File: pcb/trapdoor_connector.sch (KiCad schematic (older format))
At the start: 1 part, among them X1 A1200_trapdoor_connector

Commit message: Some work done on the whole project
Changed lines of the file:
@@
 Text Label 1100 5800 0    50   ~ 0
 _BR
-Text Label 3800 1800 0    50   ~ 0
+Text Label 3850 1800 0    50   ~ 0
 D31
-Text Label 3800 1900 0    50   ~ 0
+Text Label 3850 1900 0    50   ~ 0
 D30
-Text Label 3800 2000 0    50   ~ 0
+Text Label 3850 2000 0    50   ~ 0
 D29
 Text Label 3800 2100 0    50   ~ 0
@@
 	1    0    0    -1
 $EndComp
-Text HLabel 900  700  0    50   BiDi ~ 0
-TRPDR
-Text Label 7550 5300 0    50   ~ 0
-+5VDC
-Text Label 7550 5200 0    50   ~ 0
-+5VDC
-Text Label 7550 5100 0    50   ~ 0
-+5VDC
-Text Label 7550 4900 0    50   ~ 0
-+5VDC
-Text Label 7550 5000 0    50   ~ 0
-+5VDC
-Text Label 7550 4800 0    50   ~ 0
-+5VDC
-Text Label 7550 4700 0    50   ~ 0
-+5VDC
-Text Label 7550 4600 0    50   ~ 0
-+5VDC
-Text Label 7550 4500 0    50   ~ 0
-+5VDC
-Text Label 7550 4400 0    50   ~ 0
-+5VDC
-Text Label 7550 4300 0    50   ~ 0
+Text Label 7850 5300 0    50   ~ 0
++5VDC
+Text Label 7850 5200 0    50   ~ 0
++5VDC
+Text Label 7850 5100 0    50   ~ 0
++5VDC
+Text Label 7850 4900 0    50   ~ 0
++5VDC
+Text Label 7850 5000 0    50   ~ 0
++5VDC
+Text Label 7850 4800 0    50   ~ 0
++5VDC
+Text Label 7850 4700 0    50   ~ 0
++5VDC
+Text Label 7850 4600 0    50   ~ 0
++5VDC
+Text Label 7850 4500 0    50   ~ 0
++5VDC
+Text Label 7850 4400 0    50   ~ 0
++5VDC
+Text Label 7850 4300 0    50   ~ 0
 +5VDC
 Text Label 5050 5300 0    50   ~ 0
@@
 	4900 4700 5000 4800
 Wire Wire Line
-	7550 5300 7800 5300
-Wire Wire Line
-	7800 5200 7550 5200
-Wire Wire Line
-	7550 5100 7800 5100
-Wire Wire Line
-	7800 5000 7550 5000
-Wire Wire Line
-	7550 4900 7800 4900
-Wire Wire Line
-	7800 4800 7550 4800
-Wire Wire Line
-	7550 4700 7800 4700
-Wire Wire Line
-	7800 4600 7550 4600
-Wire Wire Line
-	7550 4500 7800 4500
-Wire Wire Line
-	7800 4400 7550 4400
-Wire Wire Line
-	7550 4300 7800 4300
+	7550 5300 8450 5300
+Wire Wire Line
+	8450 5200 7550 5200
+Wire Wire Line
+	7550 5100 8450 5100
+Wire Wire Line
+	8450 5000 7550 5000
+Wire Wire Line
+	7550 4900 8450 4900
+Wire Wire Line
+	8450 4800 7550 4800
+Wire Wire Line
+	7550 4700 8450 4700
+Wire Wire Line
+	8450 4600 7550 4600
+Wire Wire Line
+	7550 4500 8450 4500
+Wire Wire Line
+	8450 4400 7550 4400
+Wire Wire Line
+	7550 4300 8450 4300
 Wire Wire Line
 	5000 5300 5350 5300
@@
 	5000 4300 5350 4300
 Wire Bus Line
-	4900 3900 7900 3900
-Entry Wire Line
-	7800 5300 7900 5400
-Entry Wire Line
-	7800 5200 7900 5300
-Entry Wire Line
-	7800 5100 7900 5200
-Entry Wire Line
-	7800 5000 7900 5100
-Entry Wire Line
-	7800 4900 7900 5000
-Entry Wire Line
-	7800 4800 7900 4900
-Entry Wire Line
-	7800 4700 7900 4800
-Entry Wire Line
-	7800 4600 7900 4700
-Entry Wire Line
-	7800 4500 7900 4600
-Entry Wire Line
-	7800 4400 7900 4500
-Entry Wire Line
-	7800 4300 7900 4400
+	4900 3900 8550 3900
+Entry Wire Line
+	8450 5300 8550 5400
+Entry Wire Line
+	8450 5200 8550 5300
+Entry Wire Line
+	8450 5100 8550 5200
+Entry Wire Line
+	8450 5000 8550 5100
+Entry Wire Line
+	8450 4900 8550 5000
+Entry Wire Line
+	8450 4800 8550 4900
+Entry Wire Line
+	8450 4700 8550 4800
+Entry Wire Line
+	8450 4600 8550 4700
+Entry Wire Line
+	8450 4500 8550 4600
+Entry Wire Line
+	8450 4400 8550 4500
+Entry Wire Line
+	8450 4300 8550 4400
 Entry Wire Line
 	4900 5200 5000 5300
@@
 POWER_GND
 Wire Bus Line
-	7900 3900 9750 3900
-Connection ~ 7900 3900
+	8550 3900 9750 3900
+Connection ~ 8550 3900
 Entry Wire Line
 	4900 1500 5000 1600
@@
 	4900 700  4900 3200
 Wire Bus Line
-	7900 3900 7900 5400
+	8550 3900 8550 5400
 Wire Bus Line
 	4900 3900 4900 5500
@@
 Wire Bus Line
 	1000 700  1000 5800
+Text HLabel 900  700  0    50   BiDi ~ 0
+TRPDR
 $EndSCHEMATC

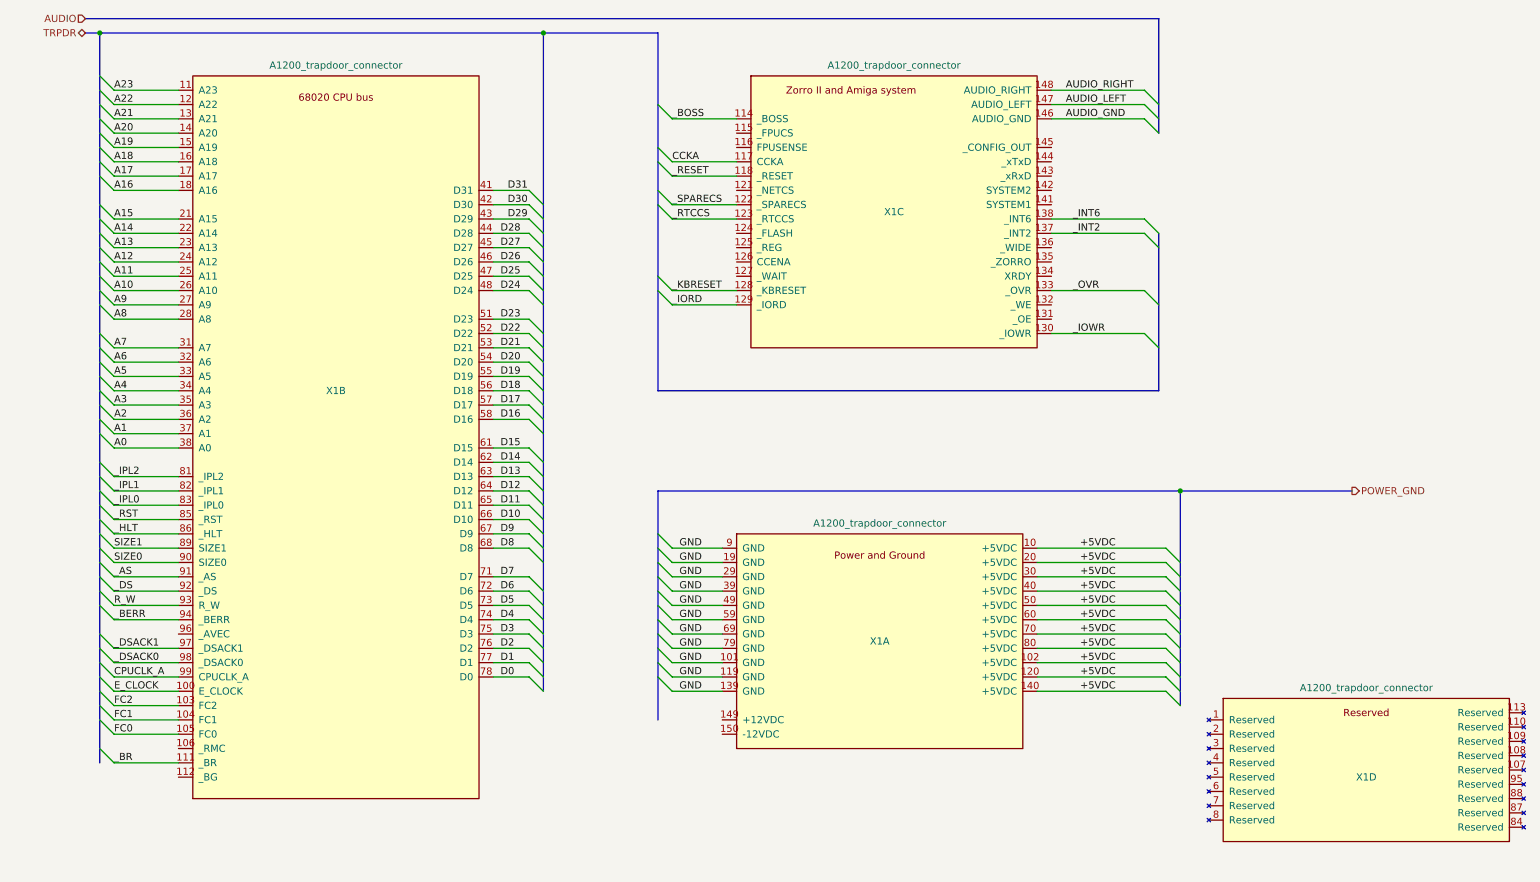
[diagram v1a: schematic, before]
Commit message: The scheme needs it's buses to be remade because of the way KiCad works, ok
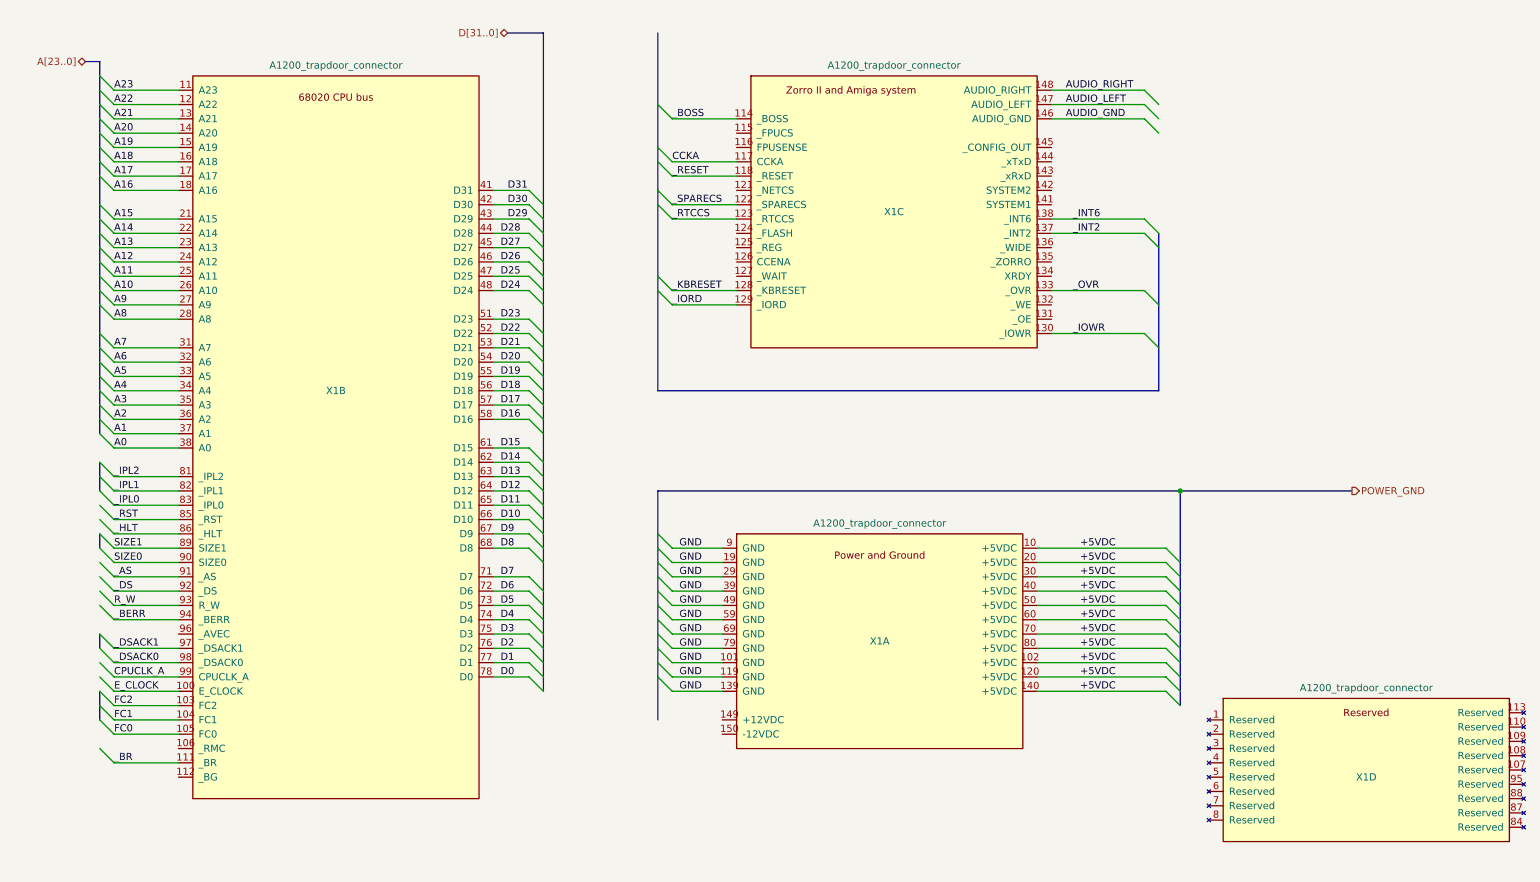
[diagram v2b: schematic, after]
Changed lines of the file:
@@
 $EndComp
 Wire Bus Line
-	900  700  1000 700
-Connection ~ 1000 700
-Wire Bus Line
-	1000 700  4100 700
-Wire Bus Line
-	4100 700  4900 700
+	900  900  1000 900
 Entry Wire Line
 	1000 1100 1100 1200
@@
 Wire Bus Line
 	4900 3200 8400 3200
-Wire Bus Line
-	8400 600  900  600
-Text HLabel 900  600  0    50   Input ~ 0
-AUDIO
-Connection ~ 4100 700
 Text HLabel 9750 3900 2    50   Output ~ 0
 POWER_GND
@@
 Text Label 1100 5300 0    50   ~ 0
 E_CLOCK
-Wire Bus Line
-	8400 600  8400 1400
+Text HLabel 900  900  0    50   BiDi ~ 0
+A[23..0]
+Wire Bus Line
+	1000 4200 1000 4300
+Wire Bus Line
+	1000 4900 1000 5000
+Text HLabel 3850 700  0    50   BiDi ~ 0
+D[31..0]
+Wire Bus Line
+	3850 700  4100 700
+Wire Bus Line
+	1000 3700 1000 3900
+Wire Bus Line
+	1000 5300 1000 5500
 Wire Bus Line
 	8400 2100 8400 3200
@@
 	4900 3900 4900 5500
 Wire Bus Line
+	1000 900  1000 3500
+Wire Bus Line
 	4100 700  4100 5300
-Wire Bus Line
-	1000 700  1000 5800
-Text HLabel 900  700  0    50   BiDi ~ 0
-TRPDR
 $EndSCHEMATC

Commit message: wip commit (sync work between pc's)
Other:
- moved on the sheet: X1A, X1B, X1C, X1D

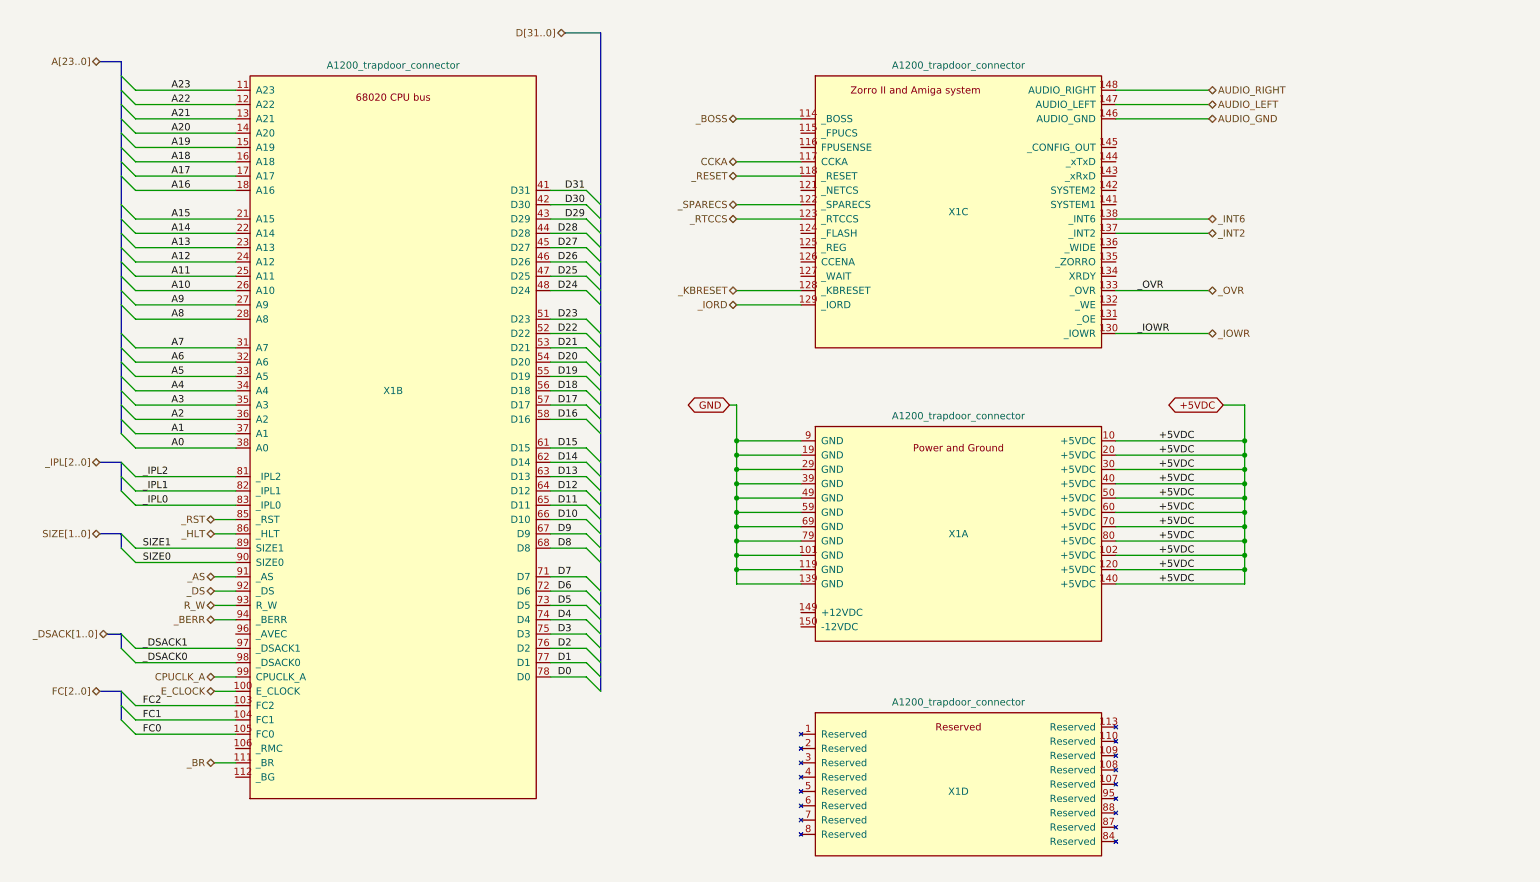
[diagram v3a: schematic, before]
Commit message: ok, we are using global labels now
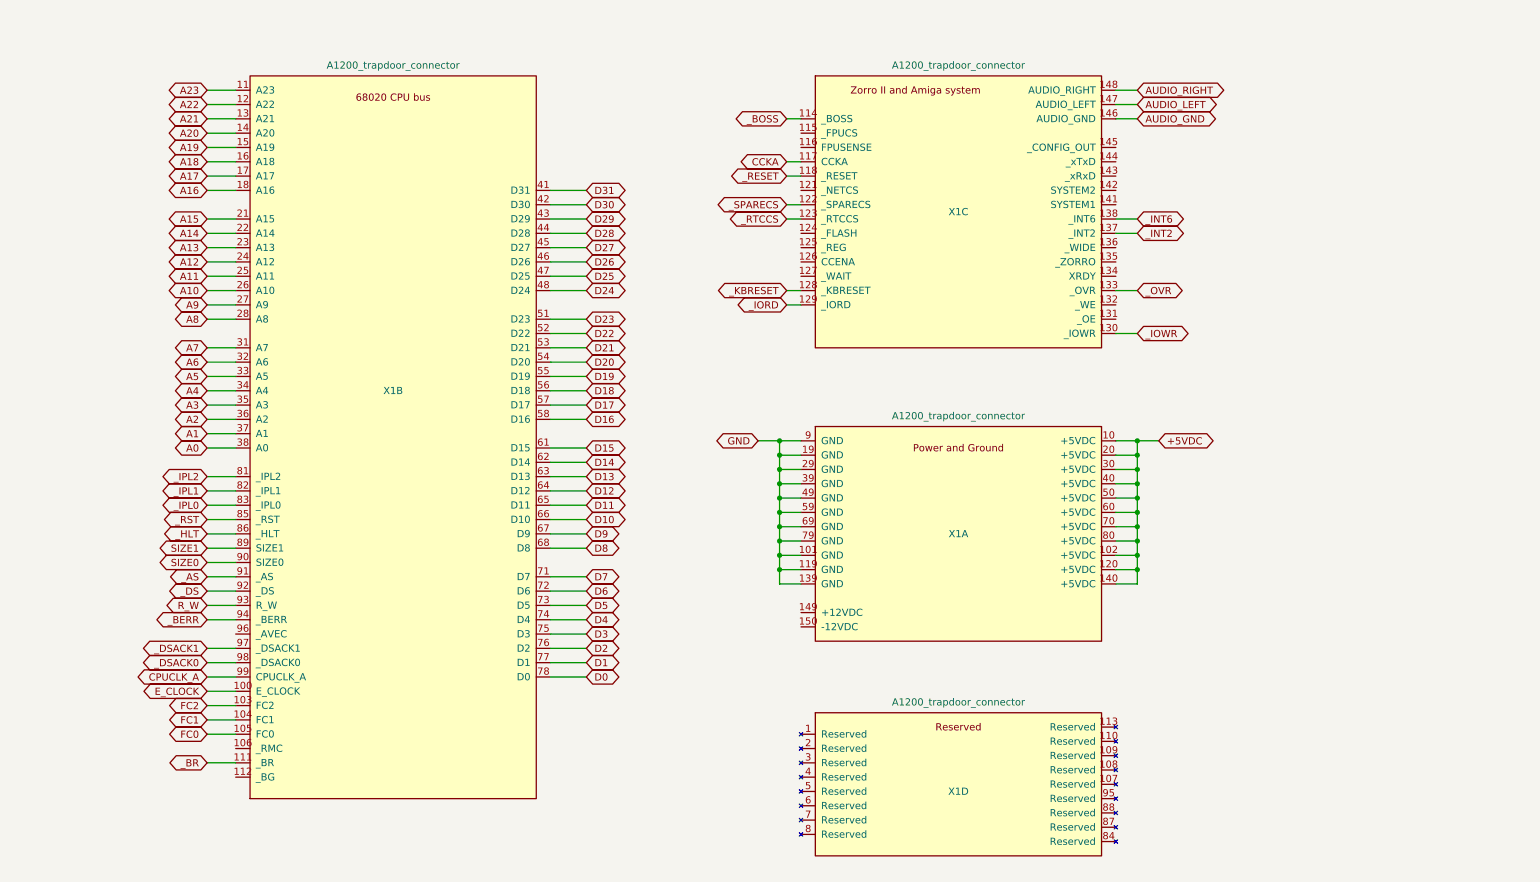
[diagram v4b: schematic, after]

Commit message: fpga-side gpio connector added
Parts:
- renumbered X1 to X3
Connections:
- net _BR is gone; now on net _BOSS: X3.111 (_BR)
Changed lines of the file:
@@
 $EndDescr
 $Comp
-L WM1200:A1200_trapdoor_connector X1
+L WM1200:A1200_trapdoor_connector X3
 U 3 1 5E6527FA
 P 7000 2900
-F 0 "X1" H 7000 3850 50  0000 C CNN
+F 0 "X3" H 7000 3850 50  0000 C CNN
 F 1 "A1200_trapdoor_connector" H 7000 4874 50  0000 C CNN
 F 2 "" H 6950 2900 50  0001 C CNN
@@
 	1950 5400 1750 5400
 $Comp
-L WM1200:A1200_trapdoor_connector X1
+L WM1200:A1200_trapdoor_connector X3
 U 2 1 5E64CEB2
 P 3050 6050
-F 0 "X1" H 3050 8900 50  0000 C CNN
+F 0 "X3" H 3050 8900 50  0000 C CNN
 F 1 "A1200_trapdoor_connector" H 3050 11174 50  0000 C CNN
 F 2 "" H 3000 6050 50  0001 C CNN
@@
 	8100 2800 8250 2800
 $Comp
-L WM1200:A1200_trapdoor_connector X1
+L WM1200:A1200_trapdoor_connector X3
 U 4 1 5E55669B
 P 7000 6450
-F 0 "X1" H 7000 6900 50  0000 C CNN
+F 0 "X3" H 7000 6900 50  0000 C CNN
 F 1 "A1200_trapdoor_connector" H 7000 7524 50  0000 C CNN
 F 2 "" H 6950 6450 50  0001 C CNN
@@
 	8100 3550 8250 3550
 $Comp
-L WM1200:A1200_trapdoor_connector X1
+L WM1200:A1200_trapdoor_connector X3
 U 1 1 5E62B199
 P 7000 4950
-F 0 "X1" H 7000 5700 50  0000 C CNN
+F 0 "X3" H 7000 5700 50  0000 C CNN
 F 1 "A1200_trapdoor_connector" H 7000 6524 50  0000 C CNN
 F 2 "" H 6950 4950 50  0001 C CNN
@@
 Wire Wire Line
 	5600 3550 5750 3550
+Text GLabel 1200 6500 0    50   BiDi ~ 0
+_BOSS
+Text GLabel 1800 6500 2    50   BiDi ~ 0
+_BR
+Wire Wire Line
+	1200 6500 1800 6500
 $EndSCHEMATC

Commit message: more footprints assigned
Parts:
- X2: renamed from X3; footprint (none) -> WM1200:Trapdoor_connector
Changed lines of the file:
@@
 $EndDescr
 $Comp
-L WM1200:A1200_trapdoor_connector X3
+L WM1200:A1200_trapdoor_connector X2
 U 3 1 5E6527FA
 P 7000 2900
-F 0 "X3" H 7000 3850 50  0000 C CNN
+F 0 "X2" H 7000 3850 50  0000 C CNN
 F 1 "A1200_trapdoor_connector" H 7000 4874 50  0000 C CNN
-F 2 "" H 6950 2900 50  0001 C CNN
+F 2 "WM1200:Trapdoor_connector" H 6950 2900 50  0001 C CNN
 F 3 "" H 6950 2900 50  0001 C CNN
 	3    7000 2900
@@
 	1950 5400 1750 5400
 $Comp
-L WM1200:A1200_trapdoor_connector X3
+L WM1200:A1200_trapdoor_connector X2
 U 2 1 5E64CEB2
 P 3050 6050
-F 0 "X3" H 3050 8900 50  0000 C CNN
+F 0 "X2" H 3050 8900 50  0000 C CNN
 F 1 "A1200_trapdoor_connector" H 3050 11174 50  0000 C CNN
-F 2 "" H 3000 6050 50  0001 C CNN
+F 2 "WM1200:Trapdoor_connector" H 3000 6050 50  0001 C CNN
 F 3 "" H 3000 6050 50  0001 C CNN
 	2    3050 6050
@@
 	8100 2800 8250 2800
 $Comp
-L WM1200:A1200_trapdoor_connector X3
+L WM1200:A1200_trapdoor_connector X2
 U 4 1 5E55669B
 P 7000 6450
-F 0 "X3" H 7000 6900 50  0000 C CNN
+F 0 "X2" H 7000 6900 50  0000 C CNN
 F 1 "A1200_trapdoor_connector" H 7000 7524 50  0000 C CNN
-F 2 "" H 6950 6450 50  0001 C CNN
+F 2 "WM1200:Trapdoor_connector" H 6950 6450 50  0001 C CNN
 F 3 "" H 6950 6450 50  0001 C CNN
 	4    7000 6450
@@
 	8100 3550 8250 3550
 $Comp
-L WM1200:A1200_trapdoor_connector X3
+L WM1200:A1200_trapdoor_connector X2
 U 1 1 5E62B199
 P 7000 4950
-F 0 "X3" H 7000 5700 50  0000 C CNN
+F 0 "X2" H 7000 5700 50  0000 C CNN
 F 1 "A1200_trapdoor_connector" H 7000 6524 50  0000 C CNN
-F 2 "" H 6950 4950 50  0001 C CNN
+F 2 "WM1200:Trapdoor_connector" H 6950 4950 50  0001 C CNN
 F 3 "" H 6950 4950 50  0001 C CNN
 	1    7000 4950
